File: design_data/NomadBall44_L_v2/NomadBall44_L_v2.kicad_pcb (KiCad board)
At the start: 2 copper layers, 149 x 96.5 mm, 58 parts, among them SW1 SW_Push, SW10 SW_Push, SW11 SW_Push, SW12 SW_Push, SW13 SW_Push, SW14 SW_Push, SW15 SW_Push, SW16 SW_Push, SW17 SW_Push, SW18 SW_Push, SW19 SW_Push, SW2 SW_Push, SW20 SW_Push, SW21 SW_Push, SW22 SW_Push, SW23 SW_Push, SW24 SW_SPDT, SW3 SW_Push, SW4 SW_Push, SW5 SW_Push, SW6 SW_Push, SW7 SW_Push, SW8 SW_Push, SW9 SW_Push, U1 XIAO-nRF52840-Plus-SMD

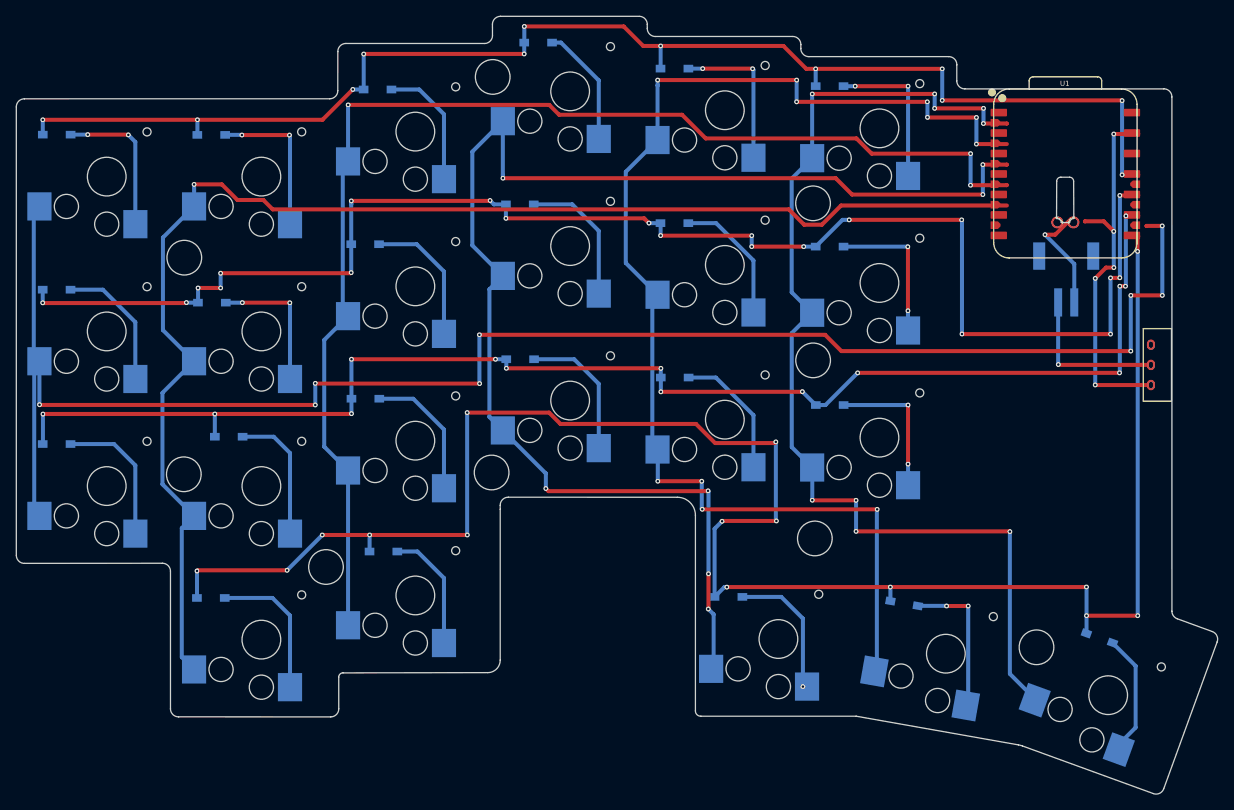
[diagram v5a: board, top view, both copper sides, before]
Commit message: 左手基板のキー位置を修正
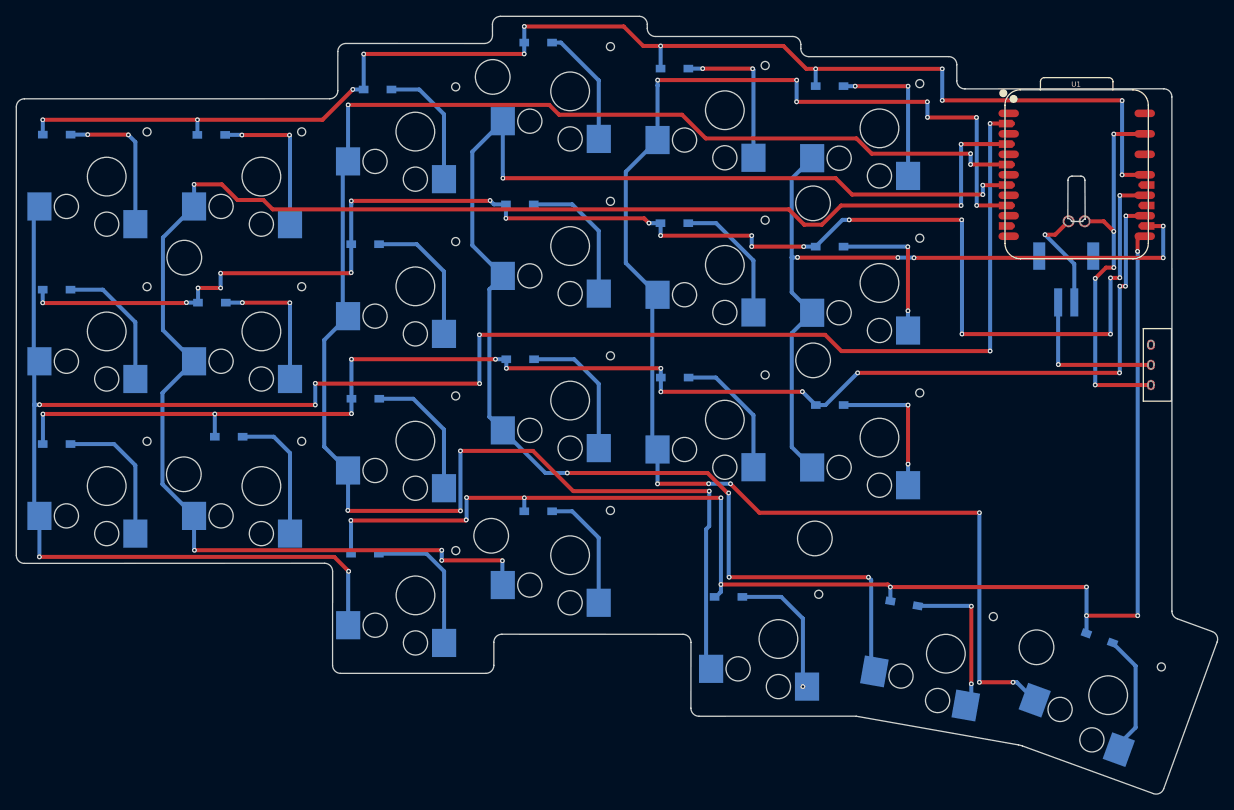
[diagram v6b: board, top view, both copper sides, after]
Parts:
- removed the REF** at (170.3, 123.5)
- U1: footprint NomadBall44:XIAO-nRF52840-Plus-ver2 -> NomadBall44:XIAO-nRF52840-Plus-ver3
- moved D19 19.9 mm to (172.4, 121.8)
- moved SW19 19.9 mm to (181.4, 127.0)
- moved D20 19.8 mm to (193.8, 116.5)
- moved SW20 19.8 mm to (200.6, 122.0)
- moved REF** 7.85 mm to (190.8, 119.6)
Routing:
- net Col0: track 344.5 -> 248.9 mm, vias 18 -> 9
- net Col5: track 0.00 -> 94.7 mm, vias 0 -> 5
- net Row3: track 229.9 -> 173.7 mm, vias 15 -> 11
- net Col1: track 155.6 -> 206.5 mm, vias 11 -> 7
- net Col2: track 169.1 -> 215.7 mm
- net Col3: track 155.7 -> 185.3 mm, vias 3 -> 7
- net Col4: track 171.8 -> 183.0 mm, vias 1 -> 13
- net Net-(D22-A): track 18.8 -> 20.4 mm
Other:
- outline, holes or cut-outs redrawn

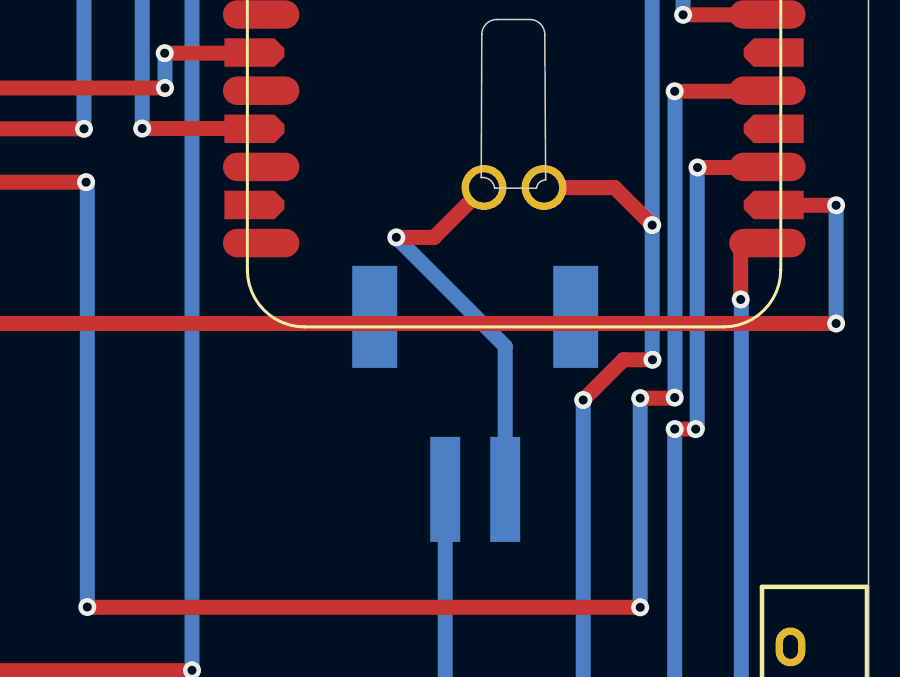
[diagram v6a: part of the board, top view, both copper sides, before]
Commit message: BAT用の配線を微修正
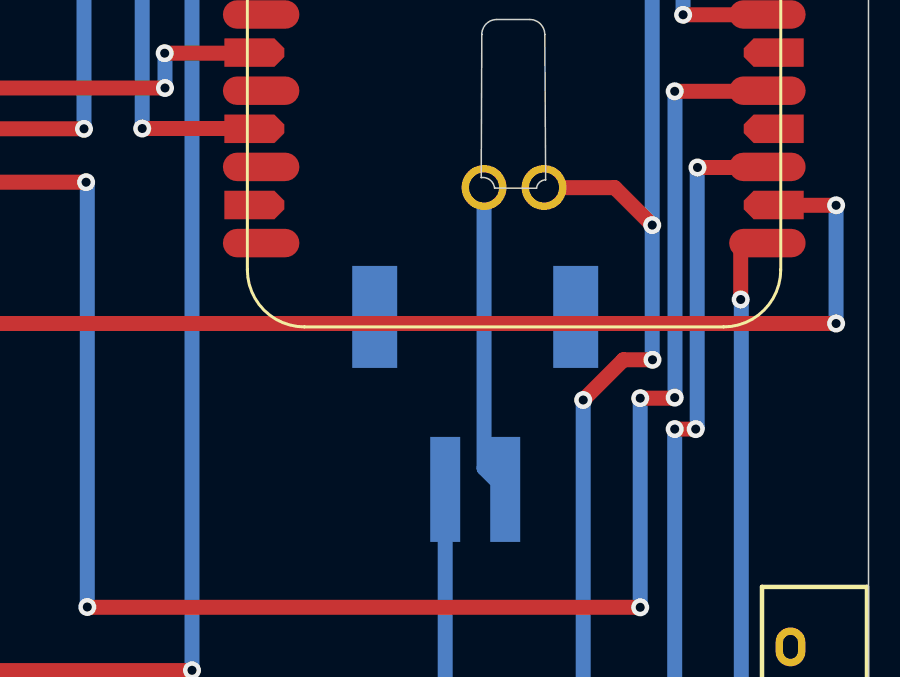
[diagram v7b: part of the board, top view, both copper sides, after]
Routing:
- net Bat: track 13.5 -> 10.4 mm, vias 1 -> 0
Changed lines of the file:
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@@
 	)
 	(segment
-		(start 259.49 82.24)
-		(end 260.751818 82.24)
-		(width 0.5)
-		(layer "F.Cu")
-		(net 1)
-	)
-	(segment
-		(start 260.751818 82.24)
-		(end 262.415 80.576818)
-		(width 0.5)
-		(layer "F.Cu")
-		(net 1)
-	)
-	(via
-		(at 259.49 82.24)
-		(size 0.6)
-		(drill 0.3)
-		(layers "F.Cu" "B.Cu")
-		(net 1)
-	)
-	(segment
-		(start 263.12 85.87)
-		(end 263.12 90.64)
+		(start 263.12 90.64)
+		(end 262.415 89.935)
 		(width 0.5)
 		(layer "B.Cu")
@@
 	)
 	(segment
-		(start 259.49 82.24)
-		(end 263.12 85.87)
+		(start 262.415 89.935)
+		(end 262.415 80.576818)
 		(width 0.5)
 		(layer "B.Cu")

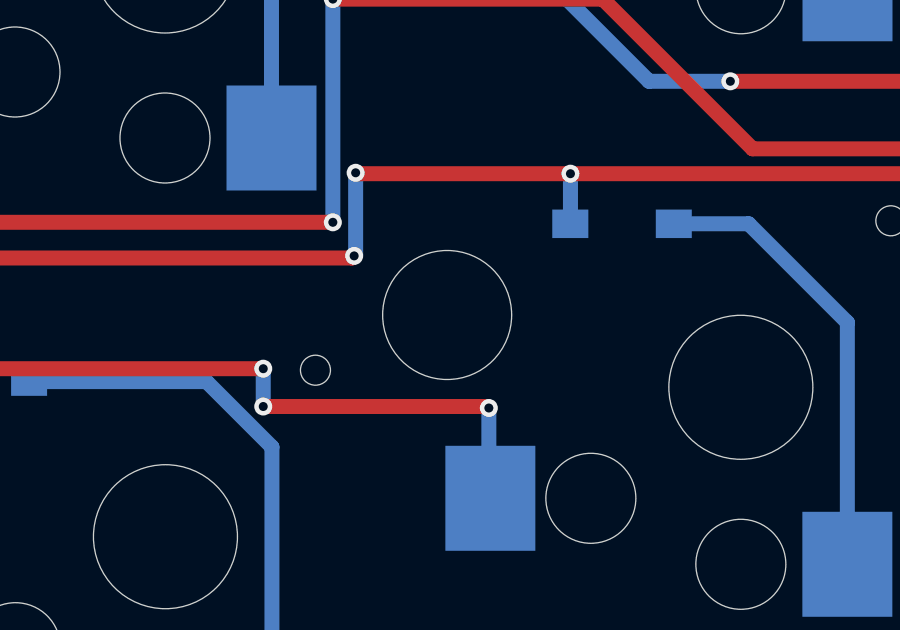
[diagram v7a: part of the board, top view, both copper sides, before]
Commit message: スペーサーの位置を微修正
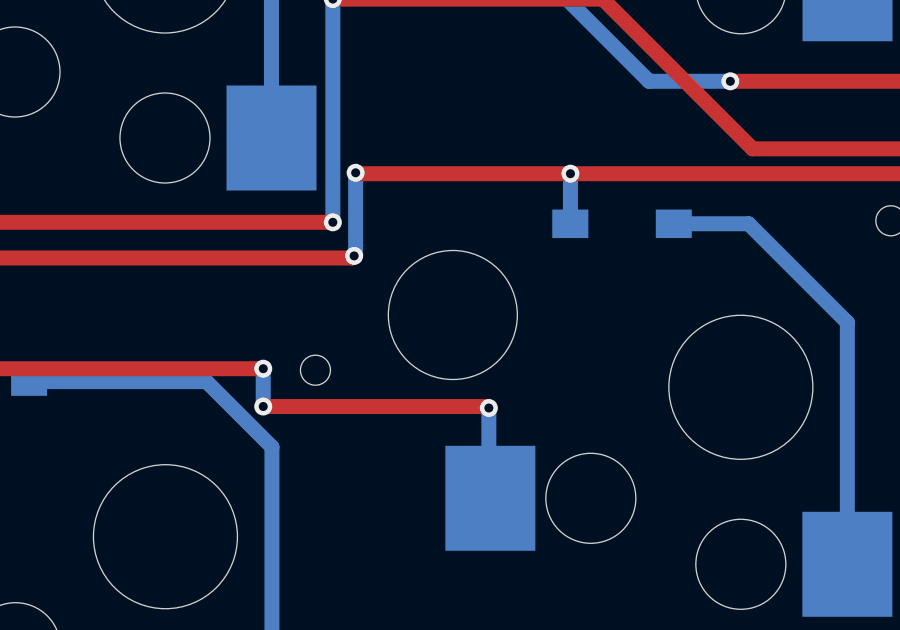
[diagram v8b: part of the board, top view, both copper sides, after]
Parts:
- moved REF** 0.19 mm to (191.0, 119.6)
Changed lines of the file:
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@@
 	(footprint "MountingHole:MountingHole_4.3mm_M4"
 		(layer "F.Cu")
-		(at 190.79 119.59)
+		(at 190.98 119.59)
 		(descr "Mounting Hole 4.3mm, M4, no annular, generated by kicad-footprint-generator mountinghole.py")
 		(tags "mountinghole M4")
